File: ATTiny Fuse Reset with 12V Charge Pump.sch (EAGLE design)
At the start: 64 parts, among them IC1 74HC04D, M1 MOUNTINGHOLE2.0, M2 MOUNTINGHOLE2.0, Q1 BSS138, Q2 PMV65XP, Q3 BSS138, Q4 BSS138, Q5 BSS138, Q6 BSS138, Q7 BSS138, Q8 BSS130, SW4 SWITCH_SPDT, U1 ARDUINOR3-BPLACE, X1 057-006-1

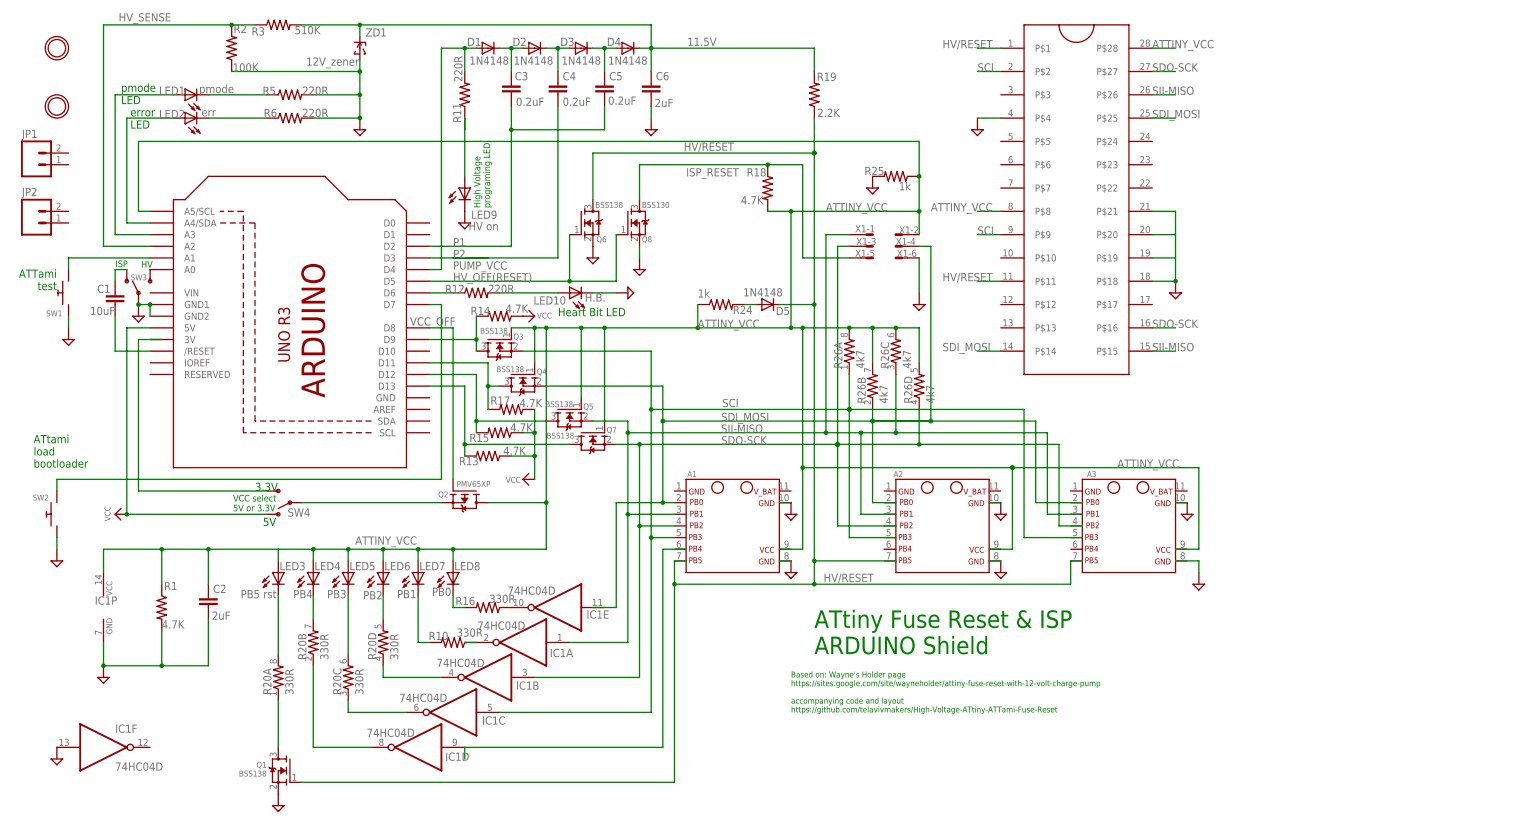
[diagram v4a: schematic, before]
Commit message: added clean arduino board, replaced attami with new parts from the lib
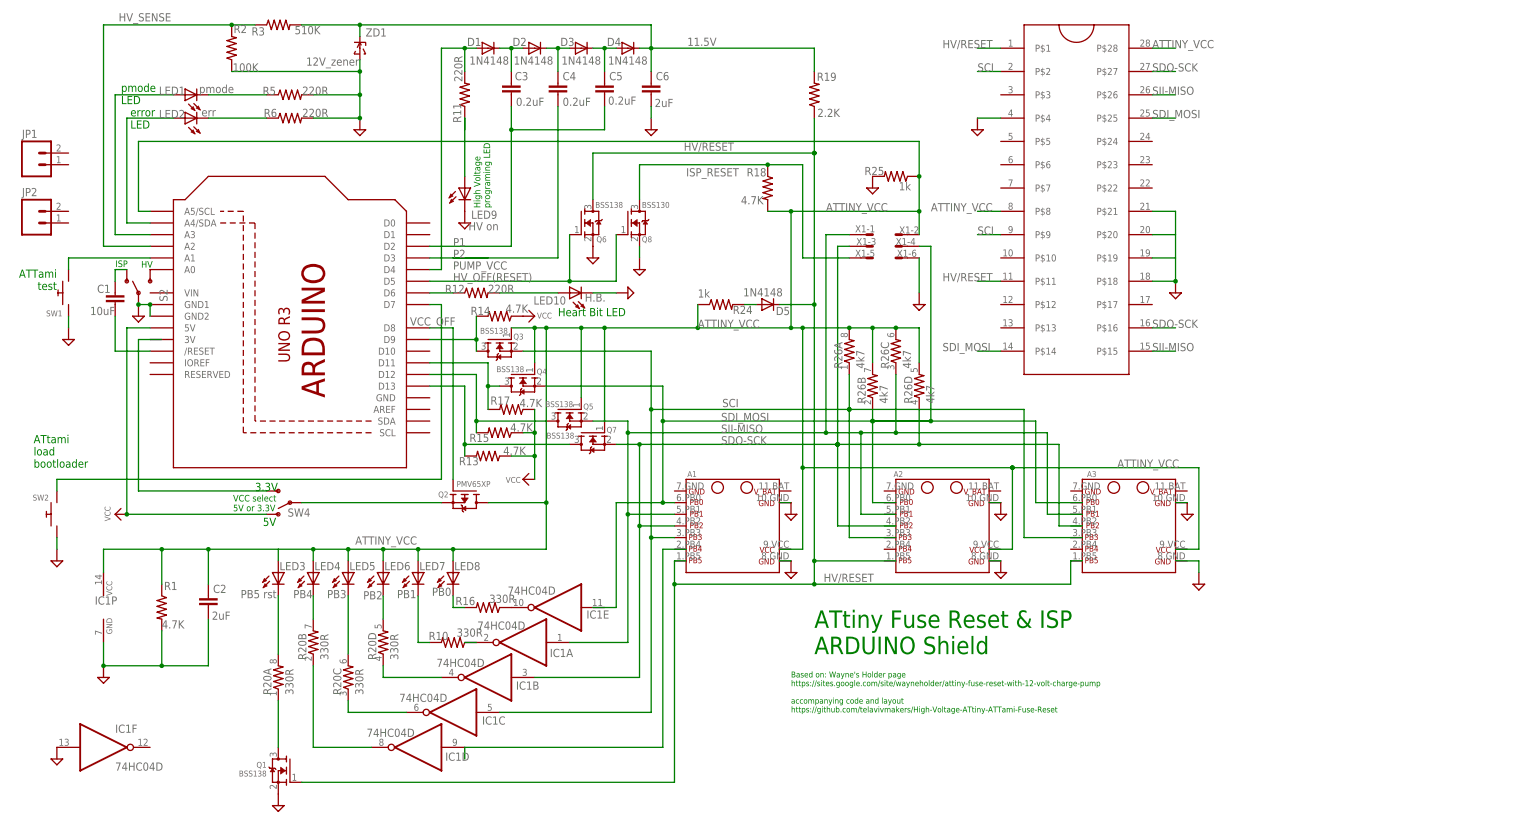
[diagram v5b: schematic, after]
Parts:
- removed M1, M2: MOUNTINGHOLE2.0, ATtami:MOUNTINGHOLE2.0
- removed SW3: (no value), microbuilder:SWITCH_SPDT
- added S2: (no value), SparkFun-Electromechanical:SWITCH-SPDTPTH
- A1, A3: device ATtami:ATTANI_BREAKOUT_PINS -> ATtami:ATTANI_BREAKOUT_PINSNOHOLE
- A2: device ATtami:ATTANI_BREAKOUT_PINS -> ATtami:ATTANI_BREAKOUT_PINSHOLES
- U1: value ARDUINOR3-BPLACE -> ARDUINOR3; device adafruit:ARDUINOR3-BPLACE -> ATtami:ARDUINOR3
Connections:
- net GND: now also S2.P; no longer SW3.P
- net N$14: now also S2.O; no longer SW3.O
- net N$3: now also S2.S; no longer SW3.S

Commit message: zif24 ito brd
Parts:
- removed R13, R14, R15, R17: 4.7K, ATtami:RESISTOR0805-RES
- removed U$1: ZIFSOCKET-28-3ZIFFSOCKET-28-3, ATTiny Fuse Reset with 12V Charge Pump:ZIFSOCKET-28-3ZIFFSOCKET-28-3
- added R4: 4k7, SparkFun-Passives:RESISTOR-ARRAY0603-ARV
- added U$2: ZIFSOCKET-24, ATTiny Fuse Reset with 12V Charge Pump:ZIFSOCKET-24
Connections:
- removed net N$50: U$1.P$20
- removed net N$51: U$1.P$19
- net ATTINY_VCC: now also U$2.P$24, U$2.P$6; no longer U$1.P$28, U$1.P$8
- net GND: now also U$2.P$16, U$2.P$17, U$2.P$18, U$2.P$19, U$2.P$4; no longer U$1.P$18, U$1.P$21, U$1.P$4
- net HV/RESET: now also U$2.P$1, U$2.P$9; no longer U$1.P$1, U$1.P$11
- net N$2: now also R4A.1; no longer R14.2
- net N$34: now also R4D.1; no longer R13.2
- net N$37: now also R4C.1; no longer R15.2
- net N$8: now also R4B.1; no longer R17.2
- net SCI: now also U$2.P$2, U$2.P$7; no longer U$1.P$2, U$1.P$9
- net SDI_MOSI: now also U$2.P$12, U$2.P$21; no longer U$1.P$14, U$1.P$25
- net SDO-SCK: now also U$2.P$14, U$2.P$23; no longer U$1.P$16, U$1.P$27
- net SII-MISO: now also U$2.P$13, U$2.P$22; no longer U$1.P$15, U$1.P$26
- net VCC: now also R4A.2, R4B.2, R4C.2, R4D.2; no longer R13.1, R14.1, R15.1, R17.1

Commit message: some more
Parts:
- renumbered LED1 to ISP, LED10 to HBEAT, LED2 to ISP_ERR, LED3 to PB5, LED4 to PB4, LED5 to PB3, LED6 to PB2, LED7 to PB1, LED8 to PB0, LED9 to HV_ON
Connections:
- removed net N$35: Q1.D, R20A.1
- removed net N$39: PB5.C, R20A.2
- new net N$31: PB5.C, R20A.1
- new net N$32: Q1.D, R20A.2
- net N$23: now also PB2.C, R20D.1; no longer PB4.C, R20B.2
- net N$24: now also R20D.2; no longer R20D.1
- net N$26: now also R20C.2; no longer R20C.1
- net N$28: now also R20B.2; no longer R20B.1
- net N$29: now also PB3.C, R20C.1; no longer PB2.C, R20D.2
- net N$30: now also PB4.C, R20B.1; no longer PB3.C, R20C.2
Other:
- moved on the sheet: R20A, R20B, R20C, R20D

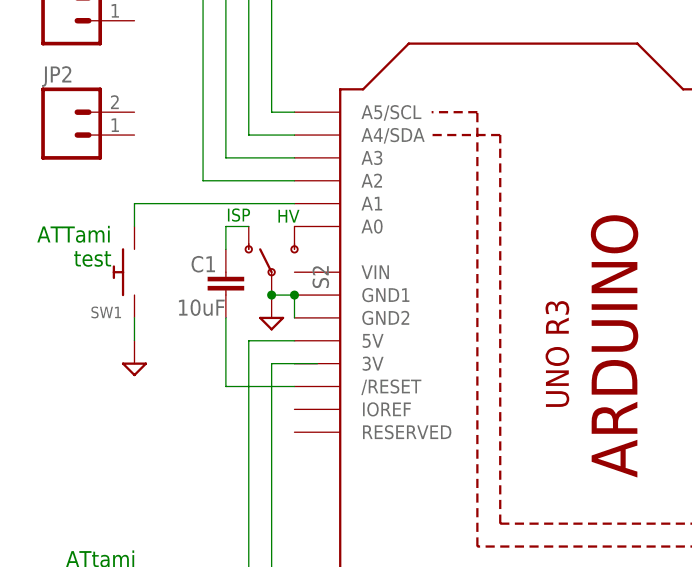
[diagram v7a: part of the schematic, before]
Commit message: removed pins from silkscreen on arduino device
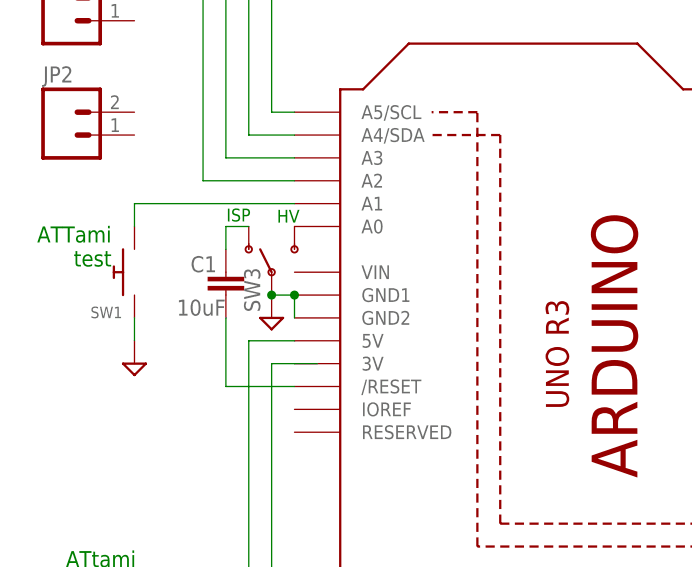
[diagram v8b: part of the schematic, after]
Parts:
- removed S2: (no value), SparkFun-Electromechanical:SWITCH-SPDTPTH
- added SW3: SWITCH_SPDT, SparkFun-Electromechanical:SWITCH_SPDT
- U1: value ARDUINOR3 -> ARDUINOR3-BPLACE; device ATtami:ARDUINOR3 -> ATtami:ARDUINOR3-BPLACE
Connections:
- net GND: now also SW3.P; no longer S2.P
- net N$14: now also SW3.O; no longer S2.O
- net N$3: now also SW3.S; no longer S2.S
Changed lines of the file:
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@@
 <grid distance="0.1" unitdist="inch" unit="inch" style="lines" multiple="1" display="no" altdistance="0.01" altunitdist="inch" altunit="inch"/>
 <layers>
-<layer number="1" name="Top" color="4" fill="1" visible="yes" active="no"/>
-<layer number="16" name="Bottom" color="1" fill="1" visible="yes" active="no"/>
-<layer number="17" name="Pads" color="2" fill="1" visible="yes" active="no"/>
-<layer number="18" name="Vias" color="2" fill="1" visible="yes" active="no"/>
-<layer number="19" name="Unrouted" color="6" fill="1" visible="yes" active="no"/>
-<layer number="20" name="Dimension" color="15" fill="1" visible="yes" active="no"/>
-<layer number="21" name="tPlace" color="16" fill="1" visible="yes" active="no"/>
-<layer number="22" name="bPlace" color="14" fill="1" visible="yes" active="no"/>
-<layer number="23" name="tOrigins" color="15" fill="1" visible="yes" active="no"/>
-<layer number="24" name="bOrigins" color="15" fill="1" visible="yes" active="no"/>
-<layer number="25" name="tNames" color="7" fill="1" visible="yes" active="no"/>
-<layer number="26" name="bNames" color="7" fill="1" visible="yes" active="no"/>
-<layer number="27" name="tValues" color="7" fill="1" visible="yes" active="no"/>
-<layer number="28" name="bValues" color="7" fill="1" visible="yes" active="no"/>
+<layer number="1" name="Top" color="4" fill="1" visible="no" active="no"/>
+<layer number="16" name="Bottom" color="1" fill="1" visible="no" active="no"/>
+<layer number="17" name="Pads" color="2" fill="1" visible="no" active="no"/>
+<layer number="18" name="Vias" color="2" fill="1" visible="no" active="no"/>
+<layer number="19" name="Unrouted" color="6" fill="1" visible="no" active="no"/>
+<layer number="20" name="Dimension" color="15" fill="1" visible="no" active="no"/>
+<layer number="21" name="tPlace" color="16" fill="1" visible="no" active="no"/>
+<layer number="22" name="bPlace" color="14" fill="1" visible="no" active="no"/>
+<layer number="23" name="tOrigins" color="15" fill="1" visible="no" active="no"/>
+<layer number="24" name="bOrigins" color="15" fill="1" visible="no" active="no"/>
+<layer number="25" name="tNames" color="7" fill="1" visible="no" active="no"/>
+<layer number="26" name="bNames" color="7" fill="1" visible="no" active="no"/>
+<layer number="27" name="tValues" color="7" fill="1" visible="no" active="no"/>
+<layer number="28" name="bValues" color="7" fill="1" visible="no" active="no"/>
 <layer number="29" name="tStop" color="7" fill="3" visible="no" active="no"/>
 <layer number="30" name="bStop" color="7" fill="6" visible="no" active="no"/>
@@
 <layer number="35" name="tGlue" color="7" fill="4" visible="no" active="no"/>
 <layer number="36" name="bGlue" color="7" fill="5" visible="no" active="no"/>
-<layer number="37" name="tTest" color="7" fill="1" visible="yes" active="no"/>
-<layer number="38" name="bTest" color="7" fill="1" visible="yes" active="no"/>
+<layer number="37" name="tTest" color="7" fill="1" visible="no" active="no"/>
+<layer number="38" name="bTest" color="7" fill="1" visible="no" active="no"/>
 <layer number="39" name="tKeepout" color="4" fill="11" visible="no" active="no"/>
 <layer number="40" name="bKeepout" color="1" fill="11" visible="no" active="no"/>
@@
 <layer number="44" name="Drills" color="7" fill="1" visible="no" active="no"/>
 <layer number="45" name="Holes" color="7" fill="1" visible="no" active="no"/>
-<layer number="46" name="Milling" color="3" fill="1" visible="yes" active="no"/>
-<layer number="47" name="Measures" color="7" fill="1" visible="yes" active="no"/>
-<layer number="48" name="Document" color="7" fill="1" visible="yes" active="no"/>
-<layer number="49" name="Reference" color="7" fill="1" visible="yes" active="no"/>
-<layer number="50" name="dxf" color="7" fill="1" visible="yes" active="no"/>
-<layer number="51" name="tDocu" color="6" fill="1" visible="yes" active="no"/>
-<layer number="52" name="bDocu" color="7" fill="1" visible="yes" active="no"/>
-<layer number="53" name="tGND_GNDA" color="7" fill="9" visible="yes" active="no"/>
-<layer number="54" name="bGND_GNDA" color="1" fill="9" visible="yes" active="no"/>
-<layer number="56" name="wert" color="7" fill="1" visible="yes" active="no"/>
-<layer number="57" name="tCAD" color="7" fill="1" visible="yes" active="no"/>
+<layer number="46" name="Milling" color="3" fill="1" visible="no" active="no"/>
+<layer number="47" name="Measures" color="7" fill="1" visible="no" active="no"/>
+<layer number="48" name="Document" color="7" fill="1" visible="no" active="no"/>
+<layer number="49" name="Reference" color="7" fill="1" visible="no" active="no"/>
+<layer number="50" name="dxf" color="7" fill="1" visible="no" active="no"/>
+<layer number="51" name="tDocu" color="6" fill="1" visible="no" active="no"/>
+<layer number="52" name="bDocu" color="7" fill="1" visible="no" active="no"/>
+<layer number="53" name="tGND_GNDA" color="7" fill="9" visible="no" active="no"/>
+<layer number="54" name="bGND_GNDA" color="1" fill="9" visible="no" active="no"/>
+<layer number="56" name="wert" color="7" fill="1" visible="no" active="no"/>
+<layer number="57" name="tCAD" color="7" fill="1" visible="no" active="no"/>
 <layer number="90" name="Modules" color="5" fill="1" visible="yes" active="yes"/>
 <layer number="91" name="Nets" color="2" fill="1" visible="yes" active="yes"/>
@@
 <part name="SUPPLY11" library="supply2" deviceset="GND" device=""/>
 <part name="FRAME1" library="frames" deviceset="DINA4_L" device=""/>
-<part name="U1" library="ATtami" deviceset="ARDUINOR3" device=""/>
+<part name="U1" library="ATtami" deviceset="ARDUINOR3" device="-BPLACE" value="ARDUINOR3-BPLACE"/>
 <part name="R11" library="ATtami" deviceset="RESISTOR" device="0805-RES" value="220R"/>
 <part name="SUPPLY7" library="supply2" deviceset="GND" device=""/>
@@
 <part name="JP1" library="SparkFun-Connectors" deviceset="M02" device="POGO_PIN_HOLES_ONLY"/>
 <part name="JP2" library="SparkFun-Connectors" deviceset="M02" device="POGO_PIN_HOLES_ONLY"/>
-<part name="S2" library="SparkFun-Electromechanical" deviceset="SWITCH-SPDT" device="PTH"/>
 <part name="R4" library="SparkFun-Passives" deviceset="RESISTOR-ARRAY" device="0603-ARV" value="4k7"/>
 <part name="U$2" library="ATTiny Fuse Reset with 12V Charge Pump" deviceset="ZIFSOCKET-24" device=""/>
+<part name="SW3" library="SparkFun-Electromechanical" deviceset="SWITCH_SPDT" device=""/>
 </parts>
 <sheets>
@@
 <attribute name="NAME" x="-317.5" y="137.922" size="1.778" layer="95"/>
 </instance>
-<instance part="S2" gate="1" x="-292.1" y="116.84" rot="R90"/>
 <instance part="R4" gate="A" x="-213.36" y="111.76"/>
 <instance part="R4" gate="B" x="-210.82" y="91.44"/>
@@
 <instance part="R4" gate="D" x="-215.9" y="81.28"/>
 <instance part="U$2" gate="G$1" x="-91.44" y="132.08"/>
+<instance part="SW3" gate="G$1" x="-292.1" y="116.84" smashed="yes" rot="R90">
+<attribute name="NAME" x="-293.37" y="112.395" size="1.778" layer="95" rot="R90"/>
+</instance>
 </instances>
 <busses>
@@
 <wire x1="-292.1" y1="114.3" x2="-289.56" y2="114.3" width="0.1524" layer="91"/>
 <junction x="-289.56" y="114.3"/>
-<pinref part="S2" gate="1" pin="P"/>
+<pinref part="SW3" gate="G$1" pin="P"/>
 <junction x="-292.1" y="114.3"/>
 </segment>
@@
 <pinref part="C1" gate="G$1" pin="1"/>
 <wire x1="-297.18" y1="121.92" x2="-297.18" y2="119.38" width="0.1524" layer="91"/>
-<pinref part="S2" gate="1" pin="O"/>
+<pinref part="SW3" gate="G$1" pin="O"/>
 </segment>
 </net>
@@
 </segment>
 </net>
-<net name="N$3" class="0">
-<segment>
-<pinref part="U1" gate="G$1" pin="A0"/>
-<pinref part="S2" gate="1" pin="S"/>
-</segment>
-</net>
 <net name="N$23" class="0">
 <segment>
@@
 </segment>
 </net>
+<net name="N$3" class="0">
+<segment>
+<pinref part="U1" gate="G$1" pin="A0"/>
+<pinref part="SW3" gate="G$1" pin="S"/>
+</segment>
+</net>
